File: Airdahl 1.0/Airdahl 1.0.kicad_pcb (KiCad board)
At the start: 2 copper layers, 57.6 x 39.5 mm, 94 parts, among them J1 Conn_01x04, J2 DF40C-34DS-0.4V_58_, J3 DF40C-34DS-0.4V_58_, J4 USB_C_Receptacle_USB2.0_16P, J7 CONUFL001-SMD-T, J9 104031-0811, SW1 SW_SPST, SW2 SW_SPST, U1 STM32F446RETx, U2 MCP2200-I-MQ, U4 BNO085, U5 BMP581, U6 RFM95W-915S2, U7 NCP1117-3.3_SOT223, Y1 ABM3B-8.000MHZ-12-D1X-T, Y2 ABS25-32.768KHZ-6-T, Y3 12MHz

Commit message: dumping many layout changes
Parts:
- removed D1, D6: RB496EATR, RB496EATR:DIO_FTZ_ROM
- removed R33: 10K, Resistor_SMD:R_0402_1005Metric
- added R38: 0, Resistor_SMD:R_0402_1005Metric, F.Cu at (160.3, 61.0)
- added R39: 0, Resistor_SMD:R_0402_1005Metric, F.Cu at (156.5, 64.7)
- added R64: 10k, Resistor_SMD:R_0402_1005Metric, F.Cu at (160.5, 65.0)
- added R65: 10k, Resistor_SMD:R_0402_1005Metric, F.Cu at (153.2, 62.0)
- added U3: LM66200DRLR, LM66200DRLR:SOT-5X3_DRL_TEX, F.Cu at (160.7, 63.0)
- added U8: LM66200DRLR, LM66200DRLR:SOT-5X3_DRL_TEX, F.Cu at (154.5, 64.6)
- C17, R54, R55: moved to F.Cu
- moved U6 66.7 mm to (136.2, 83.8)
- moved J9 60.2 mm to (172.3, 62.5), turned to -90 degrees
- moved R60 56.9 mm to (160.5, 66.2), turned to 0 degrees
- moved R53 54.0 mm to (164.0, 67.2)
- moved R54 50.8 mm to (175.1, 63.2), turned to 0 degrees
- moved BT1 49.6 mm to (139.8, 64.6), turned to 0 degrees
- moved R55 49.4 mm to (173.6, 63.0), turned to -90 degrees
- moved C13 49.1 mm to (124.8, 83.8), turned to -90 degrees
- moved R57 48.7 mm to (160.5, 65.0)
- moved R56 45.9 mm to (164.0, 68.5)
- moved R52 41.0 mm to (172.2, 70.0), turned to 0 degrees
- moved C17 40.8 mm to (175.3, 61.2)
- moved D5 35.2 mm to (133.2, 60.6)
- moved R51 35.2 mm to (133.2, 63.2)
- moved J7 34.1 mm to (124.2, 90.7), turned to -90 degrees
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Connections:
- net /PC13 renamed /PAYLOAD_S
- J2 pad 20: /PC5 -> /PAYLOAD_S1
- J2 pad 28: unconnected-(J2-Pad28) -> /PAYLOAD_S2
- J2 pad 3: unconnected-(J2-Pad3) -> +3V3
- J2 pad 7: +3V3_REG -> +3V3
- J3 pad 16: unconnected-(J3-Pad16) -> +3V3_REG
- J3 pad 20: unconnected-(J3-Pad20) -> +3V3_REG
- J3 pad 24: unconnected-(J3-Pad24) -> +3V3_REG
- J3 pad 28: unconnected-(J3-Pad28) -> +3V3_REG
- U1 pad 56: /PB4 -> /PAYLOAD_S2
- U1 pad 58: /PB6 -> /PAYLOAD_S1
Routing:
- net /SDIO_CMD: track 0.00 -> 51.4 mm, vias 0 -> 3
- net /CD: track 0.00 -> 47.6 mm, vias 0 -> 6
- net /SDIO_D1: track 0.00 -> 42.5 mm, vias 0 -> 3
- net /SDIO_D0: track 0.00 -> 40.7 mm, vias 0 -> 5
- net /SCL: track 20.2 -> 59.2 mm, vias 1 -> 2
- net +3V3: track 25.9 -> 64.7 mm, vias 0 -> 5
- net /SDA: track 24.3 -> 59.4 mm, vias 3 -> 4
- net +3V3_REG: track 0.00 -> 34.8 mm, vias 0 -> 2
- net GND: track 50.2 -> 84.9 mm, vias 38 -> 51
- net /SDIO_D2: track 0.00 -> 34.2 mm, vias 0 -> 1
- net /SDIO_CLK: track 0.00 -> 34.1 mm, vias 0 -> 1
- net /NRST: track 1.78 -> 31.3 mm, vias 1 -> 2
- net /BOOT0: track 9.10 -> 34.4 mm
- net Net-(U1-PC11): track 0.00 -> 19.7 mm, vias 0 -> 1
- net /SDIO_D3: track 0.00 -> 19.2 mm, vias 0 -> 2
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- added copper zone on F.Cu, net +3V3_REG
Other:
- board size 57.6 x 39.5 mm -> 57.6 x 40.2 mm

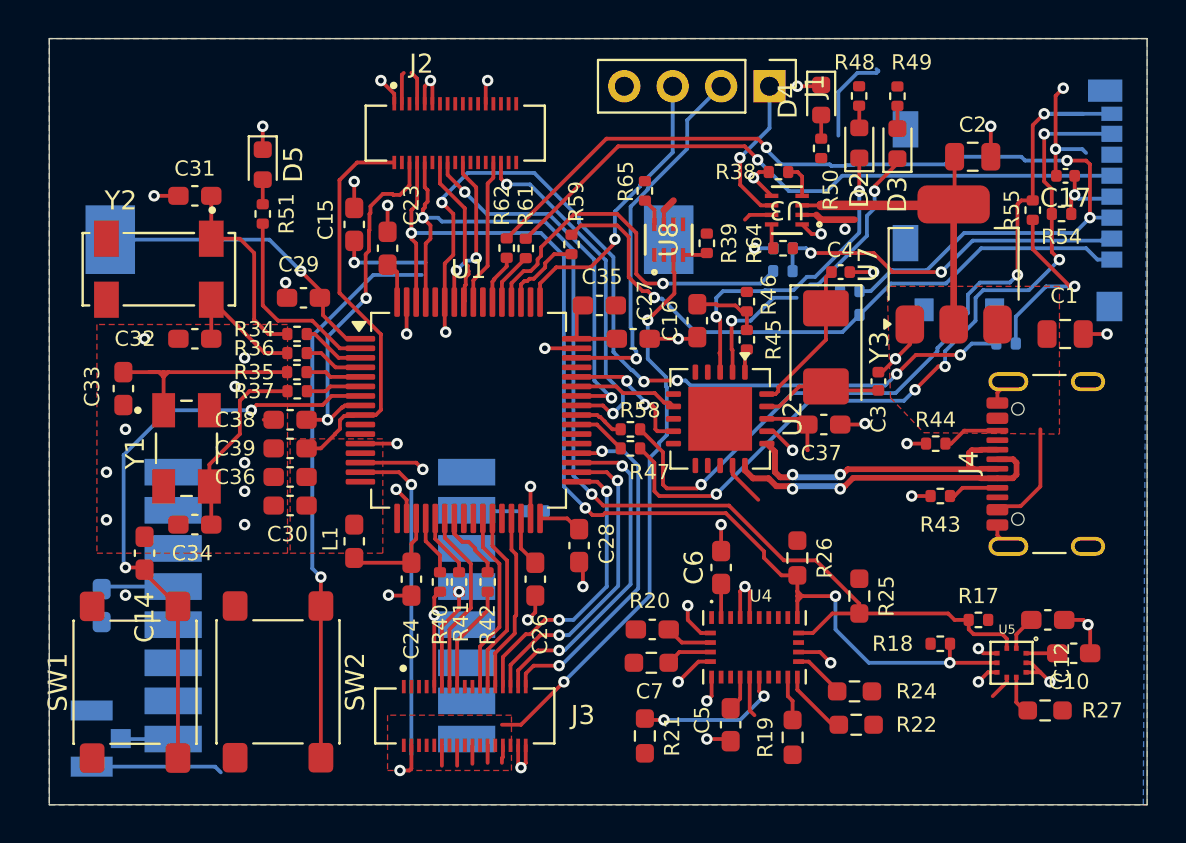
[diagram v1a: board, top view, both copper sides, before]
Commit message: mostly complete routing, just needs RFM and random IOs which are low priority
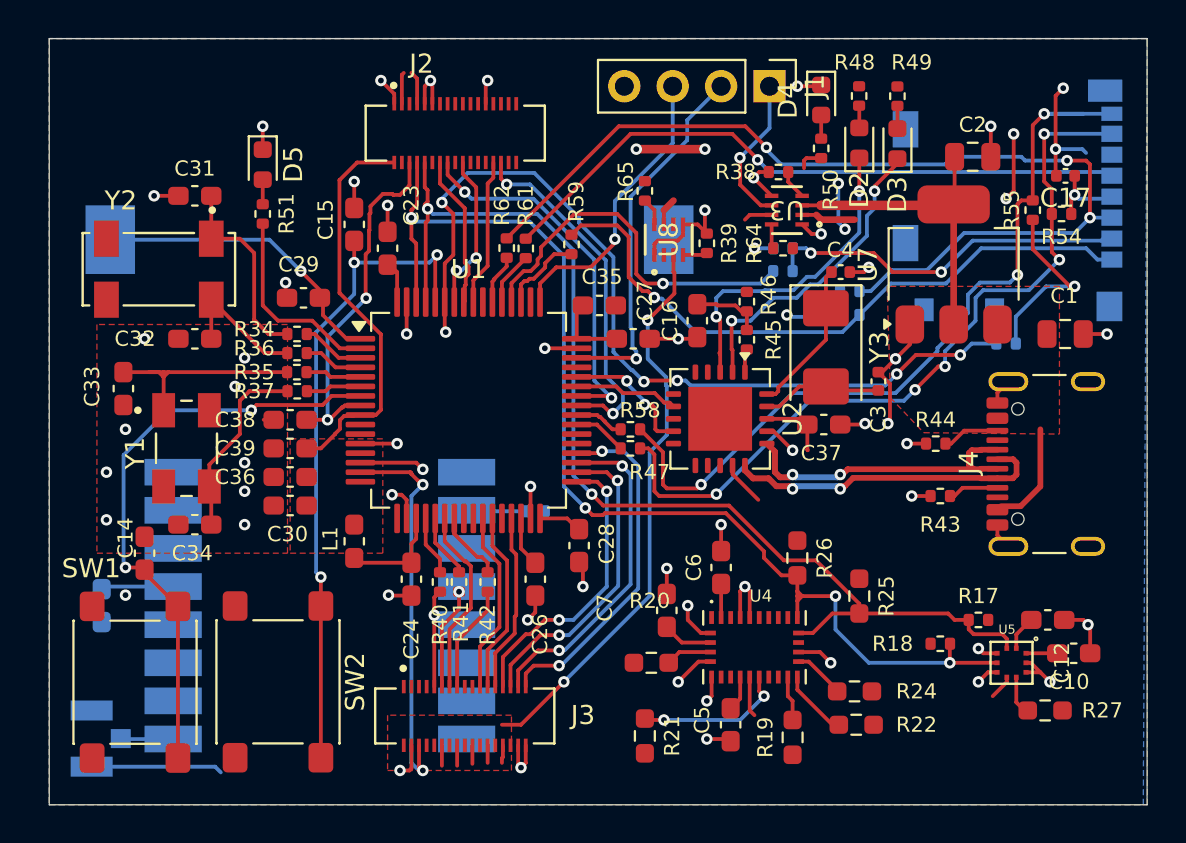
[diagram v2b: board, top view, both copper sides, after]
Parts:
- moved C7 1.26 mm to (154.4, 84.0), turned to 90 degrees
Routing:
- net GND: track 84.9 -> 101.9 mm, vias 51 -> 58
- net /PA1: track 17.1 -> 20.6 mm, vias 1 -> 2
- net +3V3: track 64.7 -> 66.5 mm, vias 5 -> 7
- net Net-(D3-K): track 15.4 -> 16.4 mm
- net /BOOT0: track 34.4 -> 35.2 mm, vias 2 -> 3
